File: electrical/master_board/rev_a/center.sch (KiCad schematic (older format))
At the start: 4 parts

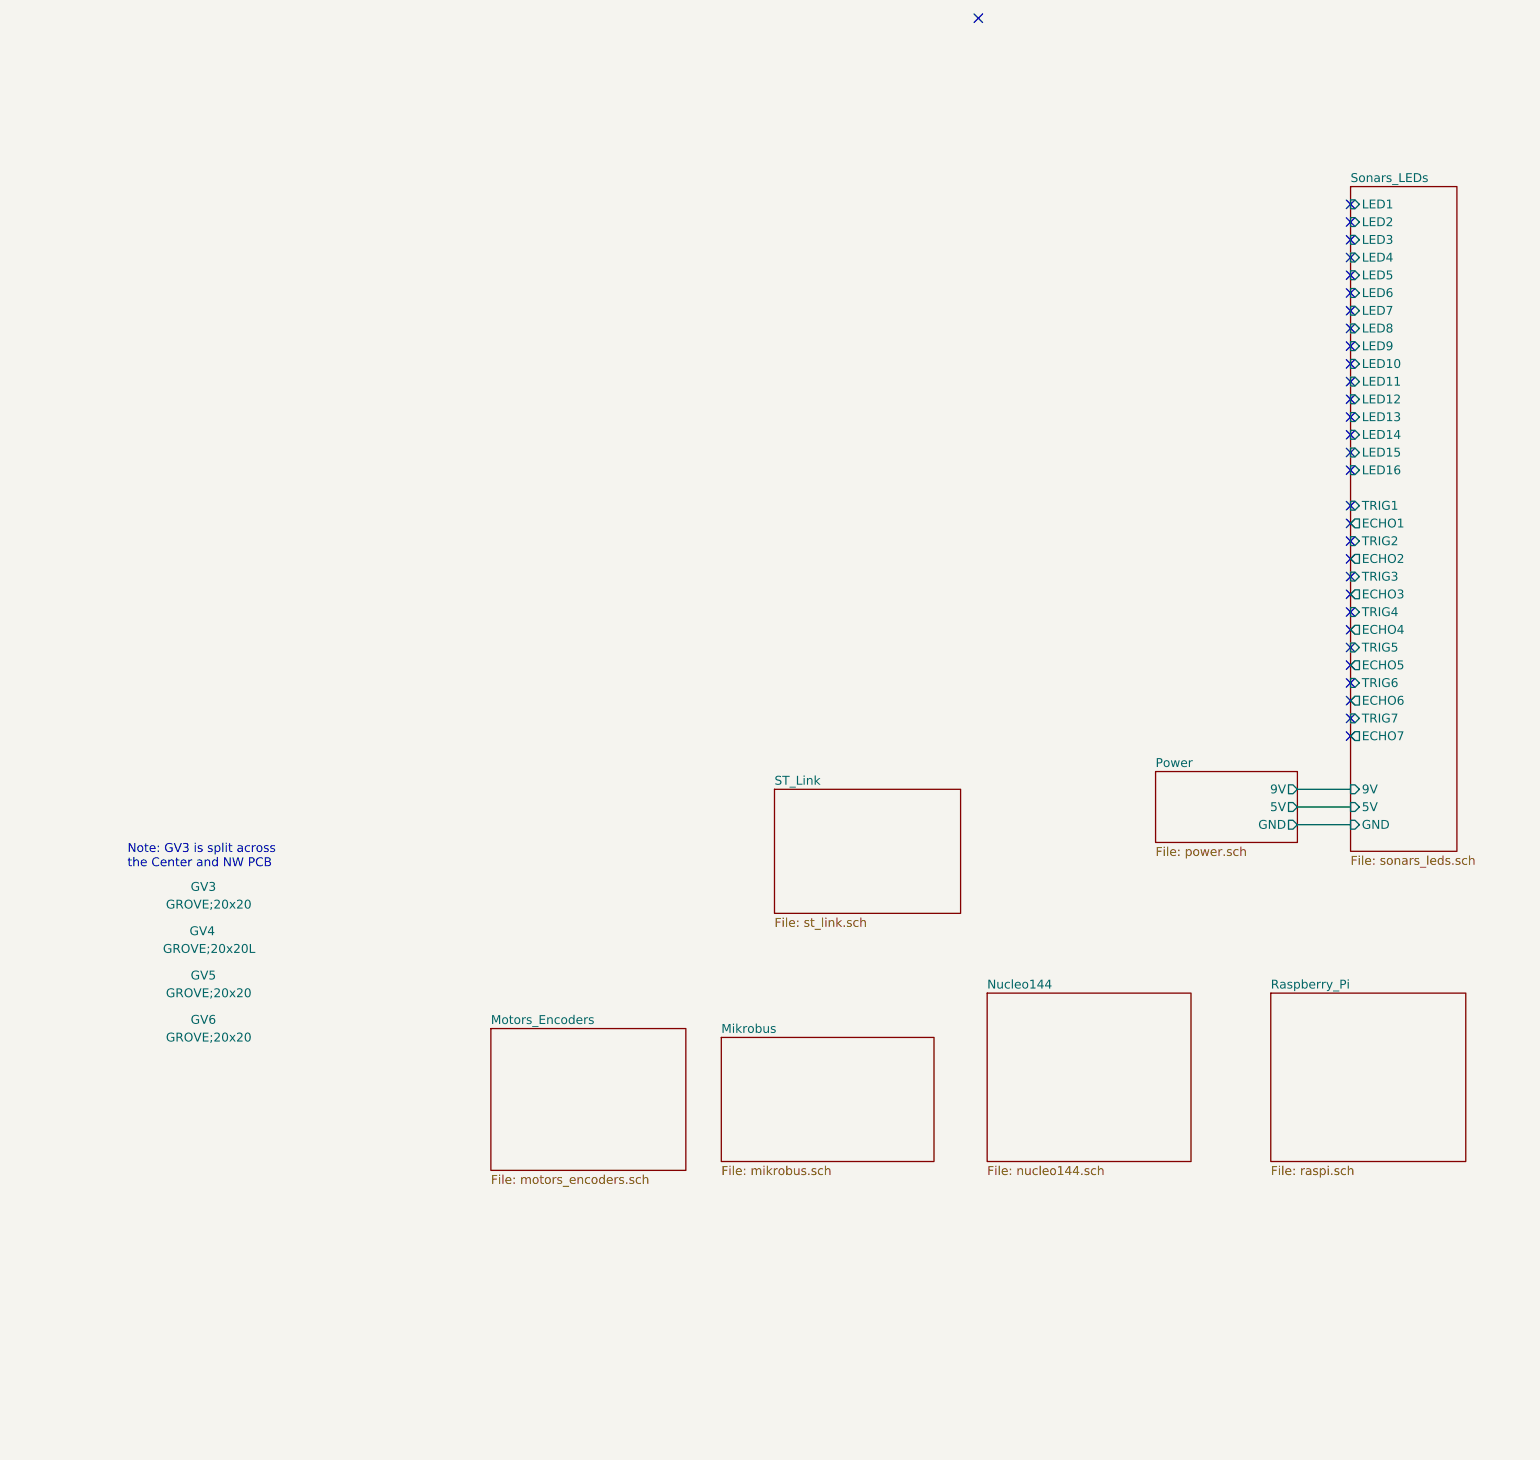
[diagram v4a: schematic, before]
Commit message: Mostly wrapped up power supply and motor driver schematics.
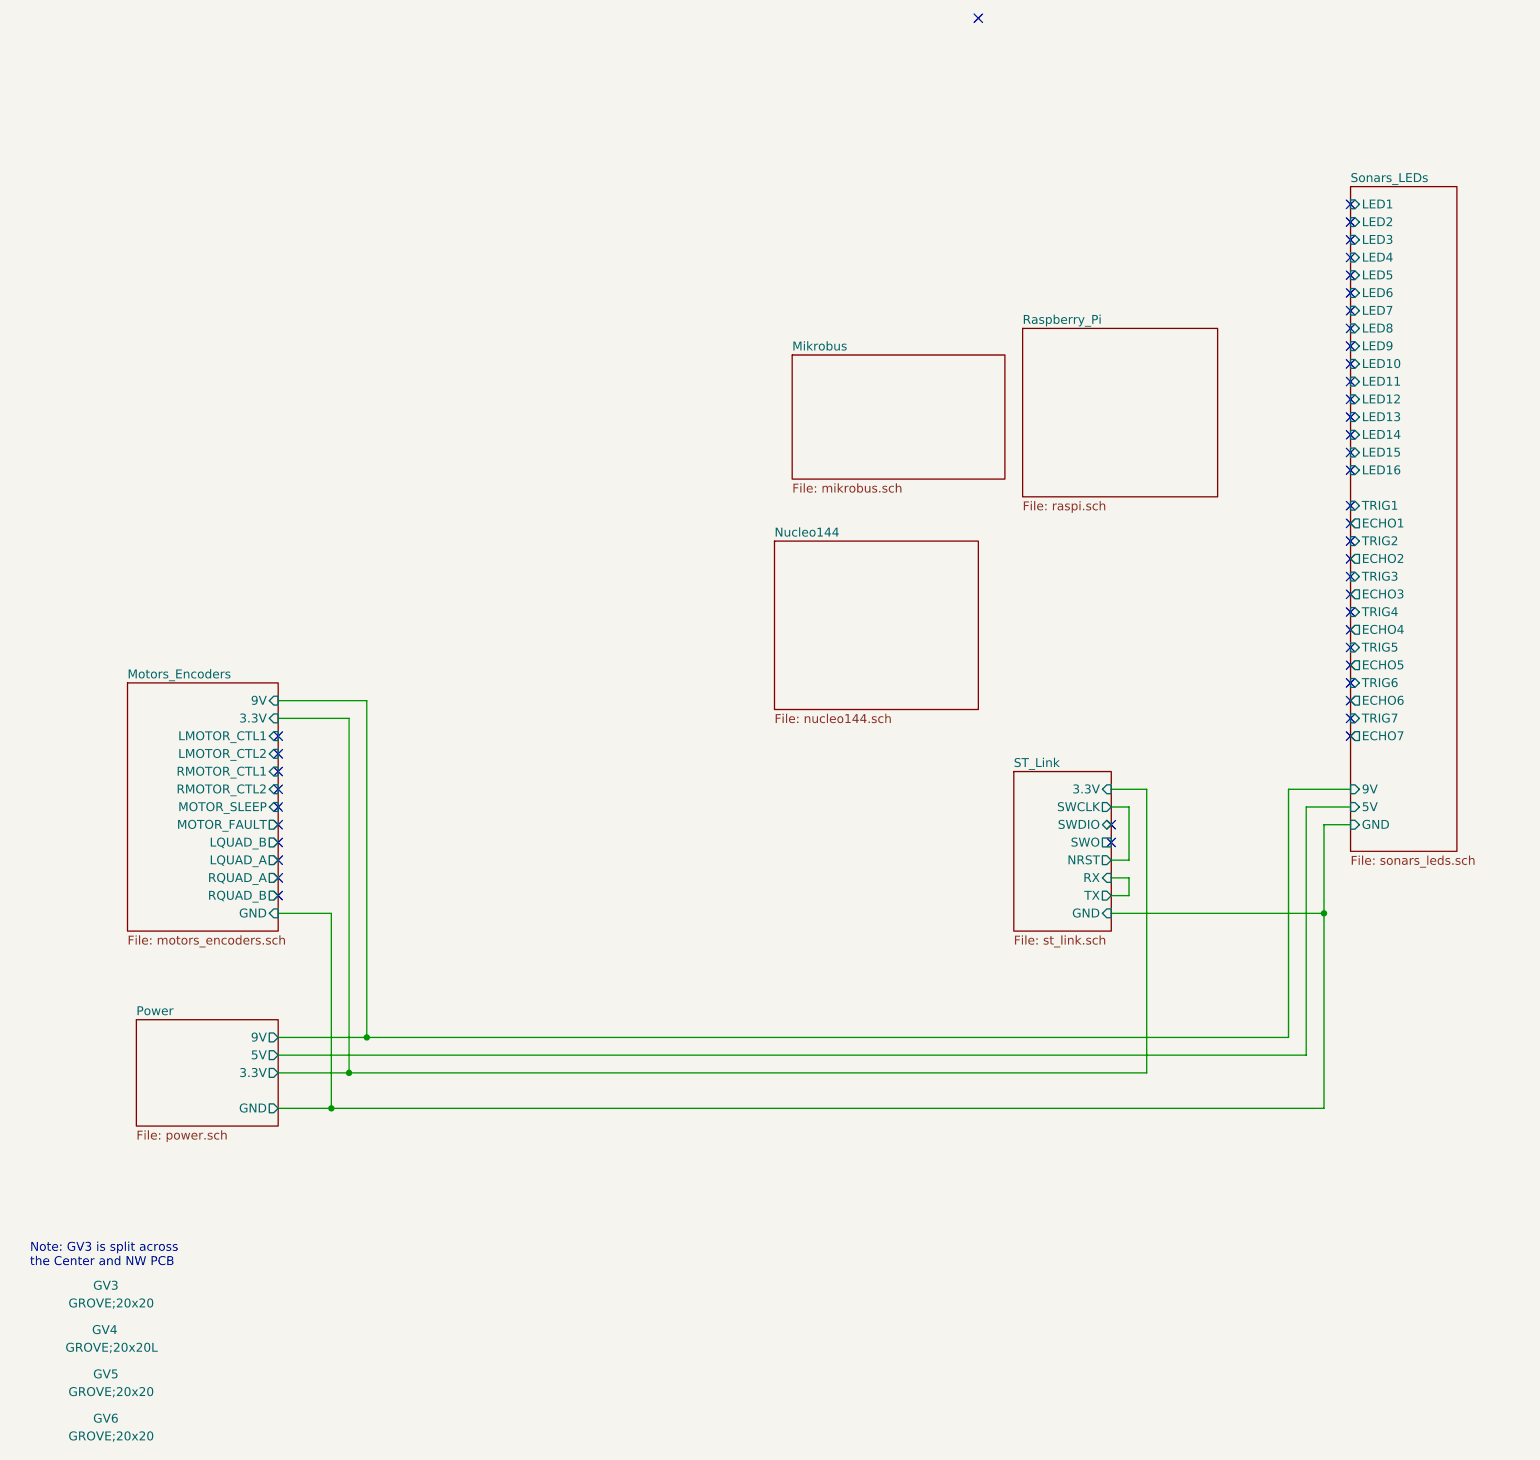
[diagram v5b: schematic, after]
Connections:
- no-connect marks 31 -> 43
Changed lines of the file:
@@
 L HR2:GROVE;20x20 GV5
 U 1 1 5F304369
-P 1600 5300
-F 0 "GV5" H 1550 5350 50  0000 L CNN
-F 1 "GROVE;20x20" H 1350 5250 50  0000 L CNN
-F 2 "HR2:GROVE20x20" H 1800 5350 60  0001 L CNN
-F 3 "Grove 20x20 Module" H 1800 5150 60  0001 L CNN
-F 4 "Grove 20x20 Module" H 1800 5250 60  0001 L CNN "manf#"
-	1    1600 5300
+P 1050 7550
+F 0 "GV5" H 1000 7600 50  0000 L CNN
+F 1 "GROVE;20x20" H 800 7500 50  0000 L CNN
+F 2 "HR2:GROVE20x20" H 1250 7600 60  0001 L CNN
+F 3 "Grove 20x20 Module" H 1250 7400 60  0001 L CNN
+F 4 "Grove 20x20 Module" H 1250 7500 60  0001 L CNN "manf#"
+	1    1050 7550
 	-1   0    0    -1
 $EndComp
@@
 L HR2:GROVE;20x20 GV6
 U 1 1 5F304374
-P 1600 5550
-F 0 "GV6" H 1550 5600 50  0000 L CNN
-F 1 "GROVE;20x20" H 1350 5500 50  0000 L CNN
-F 2 "HR2:GROVE20x20" H 1800 5600 60  0001 L CNN
-F 3 "Grove 20x20 Module" H 1800 5400 60  0001 L CNN
-F 4 "Grove 20x20 Module" H 1800 5500 60  0001 L CNN "manf#"
-	1    1600 5550
+P 1050 7800
+F 0 "GV6" H 1000 7850 50  0000 L CNN
+F 1 "GROVE;20x20" H 800 7750 50  0000 L CNN
+F 2 "HR2:GROVE20x20" H 1250 7850 60  0001 L CNN
+F 3 "Grove 20x20 Module" H 1250 7650 60  0001 L CNN
+F 4 "Grove 20x20 Module" H 1250 7750 60  0001 L CNN "manf#"
+	1    1050 7800
 	-1   0    0    -1
 $EndComp
-Text Notes 1150 4650 0    50   ~ 0
+Text Notes 600  6900 0    50   ~ 0
 Note: GV3 is split across\nthe Center and NW PCB
 $Comp
 L HR2:GROVE;20x20L GV4
 U 1 1 5F30889D
-P 1600 5050
-F 0 "GV4" H 1500 5100 50  0000 L CNN
-F 1 "GROVE;20x20L" H 1350 5000 50  0000 L CNN
-F 2 "HR2:GROVE20x20L" H 1800 5100 60  0001 L CNN
-F 3 "Grove 20x20 Module" H 1800 4900 60  0001 L CNN
-F 4 "Grove 20x20 Module" H 1800 5000 60  0001 L CNN "manf#"
-	1    1600 5050
+P 1050 7300
+F 0 "GV4" H 950 7350 50  0000 L CNN
+F 1 "GROVE;20x20L" H 800 7250 50  0000 L CNN
+F 2 "HR2:GROVE20x20L" H 1250 7350 60  0001 L CNN
+F 3 "Grove 20x20 Module" H 1250 7150 60  0001 L CNN
+F 4 "Grove 20x20 Module" H 1250 7250 60  0001 L CNN "manf#"
+	1    1050 7300
 	1    0    0    -1
 $EndComp
@@
 L HR2:GROVE;20x20 GV3
 U 1 1 5F308FA7
-P 1600 4800
-F 0 "GV3" H 1550 4850 50  0000 L CNN
-F 1 "GROVE;20x20" H 1350 4750 50  0000 L CNN
-F 2 "HR2:GROVE20x20" H 1800 4850 60  0001 L CNN
-F 3 "Grove 20x20 Module" H 1800 4650 60  0001 L CNN
-F 4 "Grove 20x20 Module" H 1800 4750 60  0001 L CNN "manf#"
-	1    1600 4800
+P 1050 7050
+F 0 "GV3" H 1000 7100 50  0000 L CNN
+F 1 "GROVE;20x20" H 800 7000 50  0000 L CNN
+F 2 "HR2:GROVE20x20" H 1250 7100 60  0001 L CNN
+F 3 "Grove 20x20 Module" H 1250 6900 60  0001 L CNN
+F 4 "Grove 20x20 Module" H 1250 7000 60  0001 L CNN "manf#"
+	1    1050 7050
 	-1   0    0    -1
 $EndComp
 $Sheet
-S 6000 5350 1150 950
+S 4800 2800 1150 950
 U 5F3221A2
 F0 "Nucleo144" 50
@@
 $EndSheet
 $Sheet
-S 7600 5350 1100 950
+S 6200 1600 1100 950
 U 5F4877FA
 F0 "Raspberry_Pi" 50
@@
 $EndSheet
 $Sheet
-S 6950 4100 800  400
+S 1200 5500 800  600
 U 5F52F39E
 F0 "Power" 50
 F1 "power.sch" 50
-F2 "9V" O R 7750 4200 50
-F3 "5V" O R 7750 4300 50
-F4 "GND" O R 7750 4400 50
-$EndSheet
-Wire Wire Line
-	7750 4200 8050 4200
-Wire Wire Line
-	7750 4300 8050 4300
-Wire Wire Line
-	7750 4400 8050 4400
+F2 "9V" O R 2000 5600 50
+F3 "5V" O R 2000 5700 50
+F4 "GND" O R 2000 6000 50
+F5 "3.3V" O R 2000 5800 50
+$EndSheet
 NoConn ~ 8050 3800
 NoConn ~ 8050 3900
 $Sheet
-S 4500 5600 1200 700
+S 4900 1750 1200 700
 U 5F4CEE66
 F0 "Mikrobus" 50
@@
 $EndSheet
 $Sheet
-S 3200 5550 1100 800
+S 1150 3600 850  1400
 U 5F4A826A
 F0 "Motors_Encoders" 50
 F1 "motors_encoders.sch" 50
-$EndSheet
-$Sheet
-S 4800 4200 1050 700
+F2 "LMOTOR_CTL2" I R 2000 4000 50
+F3 "RMOTOR_CTL2" I R 2000 4200 50
+F4 "RMOTOR_CTL1" I R 2000 4100 50
+F5 "9V" I R 2000 3700 50
+F6 "LMOTOR_CTL1" I R 2000 3900 50
+F7 "MOTOR_SLEEP" I R 2000 4300 50
+F8 "MOTOR_FAULT" O R 2000 4400 50
+F9 "3.3V" I R 2000 3800 50
+F10 "LQUAD_B" O R 2000 4500 50
+F11 "LQUAD_A" O R 2000 4600 50
+F12 "RQUAD_A" O R 2000 4700 50
+F13 "RQUAD_B" O R 2000 4800 50
+F14 "GND" I R 2000 4900 50
+$EndSheet
+$Sheet
+S 6150 4100 550  900
 U 5F4A9AB5
 F0 "ST_Link" 50
 F1 "st_link.sch" 50
-$EndSheet
+F2 "3.3V" I R 6700 4200 50
+F3 "SWCLK" O R 6700 4300 50
+F4 "GND" I R 6700 4900 50
+F5 "SWDIO" B R 6700 4400 50
+F6 "NRST" O R 6700 4600 50
+F7 "SWO" U R 6700 4500 50
+F8 "RX" I R 6700 4700 50
+F9 "TX" O R 6700 4800 50
+$EndSheet
+Wire Wire Line
+	6700 4900 7900 4900
+Wire Wire Line
+	7900 4400 8050 4400
+Wire Wire Line
+	6700 4800 6800 4800
+Wire Wire Line
+	6800 4800 6800 4700
+Wire Wire Line
+	6800 4700 6700 4700
+NoConn ~ 6700 4500
+NoConn ~ 6700 4400
+Wire Wire Line
+	6700 4300 6800 4300
+Wire Wire Line
+	6800 4300 6800 4600
+Wire Wire Line
+	6800 4600 6700 4600
+Wire Wire Line
+	2000 5600 2500 5600
+Wire Wire Line
+	2000 6000 2300 6000
+Wire Wire Line
+	7900 6000 7900 4900
+Connection ~ 7900 4900
+Wire Wire Line
+	7900 4400 7900 4900
+Wire Wire Line
+	2000 4900 2300 4900
+Wire Wire Line
+	2300 4900 2300 6000
+Connection ~ 2300 6000
+Wire Wire Line
+	2300 6000 7900 6000
+Wire Wire Line
+	2000 5800 2400 5800
+Wire Wire Line
+	2000 3800 2400 3800
+Wire Wire Line
+	2400 3800 2400 5800
+Wire Wire Line
+	2500 5600 2500 3700
+Wire Wire Line
+	2500 3700 2000 3700
+Connection ~ 2500 5600
+Wire Wire Line
+	2500 5600 7700 5600
+Wire Wire Line
+	2000 5700 7800 5700
+Wire Wire Line
+	7800 5700 7800 4300
+Wire Wire Line
+	7800 4300 8050 4300
+Wire Wire Line
+	2400 5800 6900 5800
+Wire Wire Line
+	6900 5800 6900 4200
+Connection ~ 2400 5800
+Wire Wire Line
+	7700 5600 7700 4200
+Wire Wire Line
+	7700 4200 8050 4200
+Wire Wire Line
+	6700 4200 6900 4200
+NoConn ~ 2000 4500
+NoConn ~ 2000 4600
+NoConn ~ 2000 4700
+NoConn ~ 2000 4800
+NoConn ~ 2000 4100
+NoConn ~ 2000 4300
+NoConn ~ 2000 4200
+NoConn ~ 2000 3900
+NoConn ~ 2000 4000
+NoConn ~ 2000 4400
 $EndSCHEMATC

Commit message: Wrapped up the first pass through Single Board Computer (i.e. Ras Pi)
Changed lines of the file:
@@
 	-1   0    0    -1
 $EndComp
-Text Notes 600  6900 0    50   ~ 0
+Text Notes 1500 6900 0    50   ~ 0
 Note: GV3 is split across\nthe Center and NW PCB
 $Comp
@@
 F0 "Nucleo144" 50
 F1 "nucleo144.sch" 50
-$EndSheet
-$Sheet
-S 6200 1600 1100 950
-U 5F4877FA
-F0 "Raspberry_Pi" 50
-F1 "raspi.sch" 50
 $EndSheet
 NoConn ~ 5950 -150
@@
 F28 "TRIG7" I L 8050 3800 50
 F29 "ECHO7" O L 8050 3900 50
-F30 "9V" I L 8050 4200 50
-F31 "5V" I L 8050 4300 50
-F32 "GND" I L 8050 4400 50
+F30 "9V" I R 8650 4200 50
+F31 "5V" I R 8650 4300 50
+F32 "GND" I R 8650 4400 50
 F33 "TRIG1" I L 8050 2600 50
 F34 "ECHO1" O L 8050 2700 50
 $EndSheet
 $Sheet
-S 1200 5500 800  600
+S 1150 5500 800  600
 U 5F52F39E
 F0 "Power" 50
 F1 "power.sch" 50
-F2 "9V" O R 2000 5600 50
-F3 "5V" O R 2000 5700 50
-F4 "GND" O R 2000 6000 50
-F5 "3.3V" O R 2000 5800 50
+F2 "9V" O L 1150 5600 50
+F3 "5V" O L 1150 5700 50
+F4 "GND" O L 1150 6000 50
+F5 "3.3V" O L 1150 5800 50
 $EndSheet
 NoConn ~ 8050 3800
@@
 F3 "RMOTOR_CTL2" I R 2000 4200 50
 F4 "RMOTOR_CTL1" I R 2000 4100 50
-F5 "9V" I R 2000 3700 50
+F5 "9V" I L 1150 3700 50
 F6 "LMOTOR_CTL1" I R 2000 3900 50
 F7 "MOTOR_SLEEP" I R 2000 4300 50
 F8 "MOTOR_FAULT" O R 2000 4400 50
-F9 "3.3V" I R 2000 3800 50
+F9 "3.3V" I L 1150 3800 50
 F10 "LQUAD_B" O R 2000 4500 50
 F11 "LQUAD_A" O R 2000 4600 50
 F12 "RQUAD_A" O R 2000 4700 50
 F13 "RQUAD_B" O R 2000 4800 50
-F14 "GND" I R 2000 4900 50
-$EndSheet
-$Sheet
-S 6150 4100 550  900
+F14 "GND" I L 1150 4900 50
+$EndSheet
+$Sheet
+S 1150 1600 550  900
 U 5F4A9AB5
 F0 "ST_Link" 50
 F1 "st_link.sch" 50
-F2 "3.3V" I R 6700 4200 50
-F3 "SWCLK" O R 6700 4300 50
-F4 "GND" I R 6700 4900 50
-F5 "SWDIO" B R 6700 4400 50
-F6 "NRST" O R 6700 4600 50
-F7 "SWO" U R 6700 4500 50
-F8 "RX" I R 6700 4700 50
-F9 "TX" O R 6700 4800 50
-$EndSheet
-Wire Wire Line
-	6700 4900 7900 4900
-Wire Wire Line
-	7900 4400 8050 4400
-Wire Wire Line
-	6700 4800 6800 4800
-Wire Wire Line
-	6800 4800 6800 4700
-Wire Wire Line
-	6800 4700 6700 4700
-NoConn ~ 6700 4500
-NoConn ~ 6700 4400
-Wire Wire Line
-	6700 4300 6800 4300
-Wire Wire Line
-	6800 4300 6800 4600
-Wire Wire Line
-	6800 4600 6700 4600
-Wire Wire Line
-	2000 5600 2500 5600
-Wire Wire Line
-	2000 6000 2300 6000
-Wire Wire Line
-	7900 6000 7900 4900
-Connection ~ 7900 4900
-Wire Wire Line
-	7900 4400 7900 4900
-Wire Wire Line
-	2000 4900 2300 4900
-Wire Wire Line
-	2300 4900 2300 6000
-Connection ~ 2300 6000
-Wire Wire Line
-	2300 6000 7900 6000
-Wire Wire Line
-	2000 5800 2400 5800
-Wire Wire Line
-	2000 3800 2400 3800
-Wire Wire Line
-	2400 3800 2400 5800
-Wire Wire Line
-	2500 5600 2500 3700
-Wire Wire Line
-	2500 3700 2000 3700
-Connection ~ 2500 5600
-Wire Wire Line
-	2500 5600 7700 5600
-Wire Wire Line
-	2000 5700 7800 5700
-Wire Wire Line
-	7800 5700 7800 4300
-Wire Wire Line
-	7800 4300 8050 4300
-Wire Wire Line
-	2400 5800 6900 5800
-Wire Wire Line
-	6900 5800 6900 4200
-Connection ~ 2400 5800
-Wire Wire Line
-	7700 5600 7700 4200
-Wire Wire Line
-	7700 4200 8050 4200
-Wire Wire Line
-	6700 4200 6900 4200
+F2 "3.3V" I L 1150 1700 50
+F3 "SWCLK" O R 1700 1800 50
+F4 "GND" I L 1150 2400 50
+F5 "SWDIO" B R 1700 1900 50
+F6 "NRST" O R 1700 2100 50
+F7 "SWO" U R 1700 2000 50
+F8 "RX" I R 1700 2200 50
+F9 "TX" O R 1700 2300 50
+$EndSheet
+NoConn ~ 1700 2000
+NoConn ~ 1700 1900
 NoConn ~ 2000 4500
 NoConn ~ 2000 4600
@@
 NoConn ~ 2000 4000
 NoConn ~ 2000 4400
+$Sheet
+S 7550 5250 1100 500
+U 5F4877FA
+F0 "Single Board Computer" 50
+F1 "sbc.sch" 50
+F2 "SBC_TX" O L 7550 5350 50
+F3 "SBC_RX" O L 7550 5450 50
+F4 "5V" I R 8650 5350 50
+F5 "GND" I R 8650 5650 50
+F6 "3.3V" I R 8650 5450 50
+F7 "SBC_ALIVE" O L 7550 5550 50
+F8 "SBC_SHUTDOWN" I L 7550 5650 50
+$EndSheet
+Wire Bus Line
+	800  6500 9000 6500
+Wire Wire Line
+	1150 3700 900  3700
+Entry Wire Line
+	800  3800 900  3700
+Text Label 950  3700 0    50   ~ 0
+9V
+Text Label 950  3800 0    50   ~ 0
+3.3V
+Wire Wire Line
+	1150 3800 900  3800
+Entry Wire Line
+	800  3900 900  3800
+Text Label 950  4900 0    50   ~ 0
+GND
+Wire Wire Line
+	1150 4900 900  4900
+Entry Wire Line
+	800  5000 900  4900
+Wire Wire Line
+	1150 5600 900  5600
+Entry Wire Line
+	800  5700 900  5600
+Text Label 950  5600 0    50   ~ 0
+9V
+Text Label 950  5700 0    50   ~ 0
+5V
+Wire Wire Line
+	1150 5700 900  5700
+Entry Wire Line
+	800  5800 900  5700
+Text Label 950  6000 0    50   ~ 0
+GND
+Wire Wire Line
+	1150 6000 900  6000
+Entry Wire Line
+	800  6100 900  6000
+Text Label 950  5800 0    50   ~ 0
+3.3V
+Wire Wire Line
+	1150 5800 900  5800
+Entry Wire Line
+	800  5900 900  5800
+Wire Wire Line
+	1700 2300 1800 2300
+Wire Wire Line
+	1800 2200 1700 2200
+Wire Wire Line
+	1800 2300 1800 2200
+Wire Wire Line
+	1800 2100 1700 2100
+Wire Wire Line
+	1700 1800 1800 1800
+Wire Wire Line
+	1800 1800 1800 2100
+Text Label 950  1700 0    50   ~ 0
+3.3V
+Wire Wire Line
+	1150 1700 900  1700
+Entry Wire Line
+	800  1800 900  1700
+Wire Wire Line
+	1150 2400 900  2400
+Entry Wire Line
+	800  2500 900  2400
+Text Label 950  2400 0    50   ~ 0
+GND
+Wire Wire Line
+	8650 4200 8900 4200
+Wire Wire Line
+	8650 4300 8650 4400
+Wire Wire Line
+	8650 4400 8900 4400
+Wire Wire Line
+	8650 4300 8900 4300
+Entry Wire Line
+	8900 4200 9000 4300
+Entry Wire Line
+	8900 4300 9000 4400
+Entry Wire Line
+	8900 4400 9000 4500
+Text Label 8700 4200 0    50   ~ 0
+9V
+Text Label 8700 4300 0    50   ~ 0
+5V
+Text Label 8700 4400 0    50   ~ 0
+GND
+Wire Wire Line
+	8650 5350 8900 5350
+Wire Wire Line
+	8650 5450 8900 5450
+Wire Wire Line
+	8650 5650 8900 5650
+Entry Wire Line
+	8900 5350 9000 5450
+Entry Wire Line
+	8900 5450 9000 5550
+Entry Wire Line
+	8900 5650 9000 5750
+Text Label 8700 5350 0    50   ~ 0
+5V
+Text Label 8700 5650 0    50   ~ 0
+GND
+Text Label 8700 5450 0    50   ~ 0
+3.3V
+Wire Wire Line
+	7550 5350 7450 5350
+Wire Wire Line
+	7450 5350 7450 5450
+Wire Wire Line
+	7450 5450 7550 5450
+Wire Bus Line
+	800  1700 800  6500
+Wire Bus Line
+	9000 1000 9000 6500
 $EndSCHEMATC
